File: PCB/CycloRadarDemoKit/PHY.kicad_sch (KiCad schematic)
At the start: 11 parts, among them U201 IP101GRI, Y201 Crystal_GND24

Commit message: PCB PHY WIP_1
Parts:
- added D201, D202: LED, symbol Device:LED
- added R206, R209: 5.1K(5%), symbol Device:R
- added R207, R208: R, symbol Device:R
- TP202: value TXER -> RXER
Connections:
- net +3V3: now also D201.2 (A), R206.2
- net GND: now also D202.1 (K), R209.2
- net at R203.2, U201.21 (RXER/INTR_32): now also TP202.1
- net LED0/PHY_AD0: now reaches U201.11 (LED0/PHY_AD0)
- net LED0/PHY_AD0: now also R206.1, R207.2
- net LED3/PHY_AD3: now reaches U201.12 (LED3/PHY_AD3)
- net LED3/PHY_AD3: now also R208.2, R209.1
- new net: D202.2 (A), R208.1
- new net: D201.1 (K), R207.1
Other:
- note added: "TODO: Choose LED on JLC - then decide on resistor"
- note added: "TODO: Choose RC components on JLC"
- note added: "pokračovať treba pinom 13, idem ACW"
- moved on the sheet: TP201, TP202

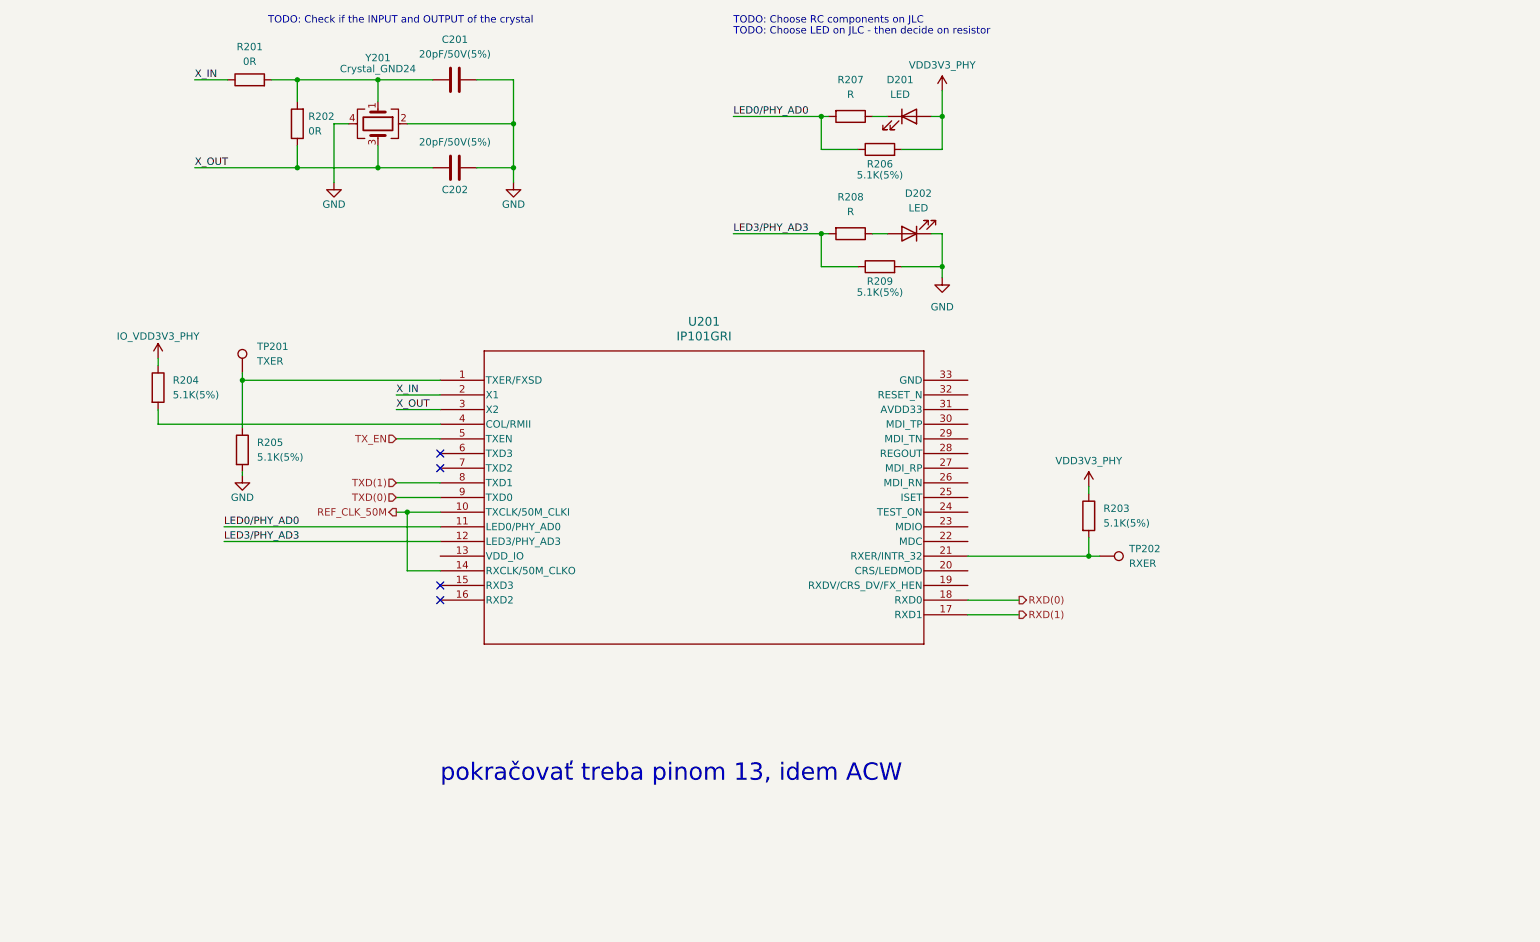
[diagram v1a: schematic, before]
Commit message: PCB WIP Started working on CP2102
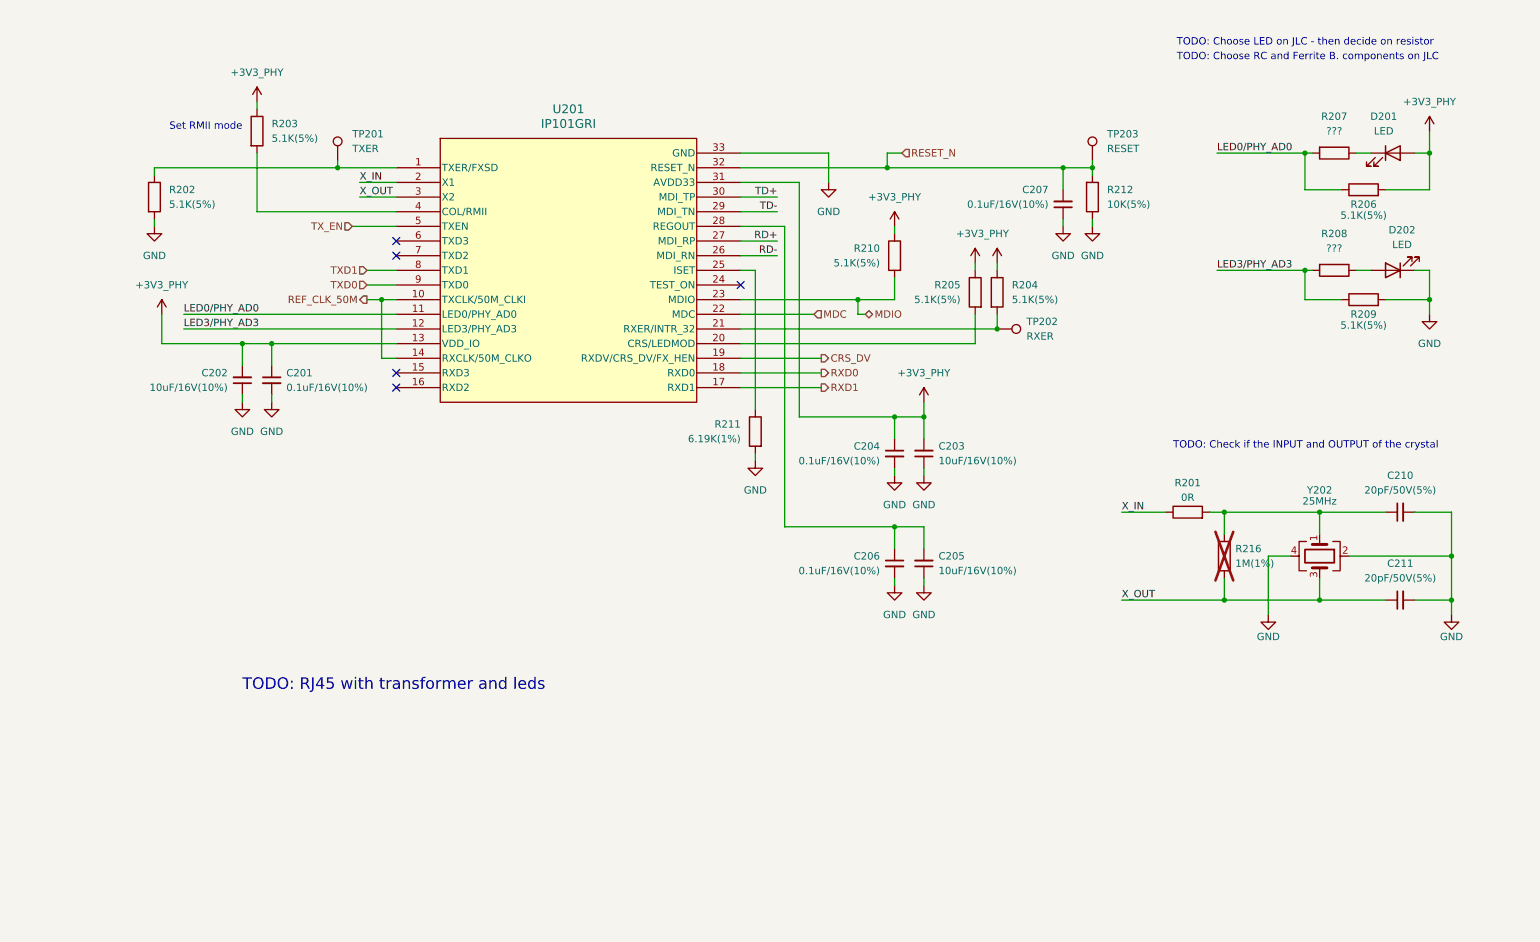
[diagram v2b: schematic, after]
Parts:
- removed C201, C202: 20pF/50V(5%), symbol Device:C
- removed Y201: Crystal_GND24, symbol Device:Crystal_GND24
- added C201, C204, C206, C207: 0.1uF/16V(10%), symbol Device:C_Small
- added C202, C203, C205: 10uF/16V(10%), symbol Device:C_Small
- added C210, C211: 20pF/50V(5%), symbol Device:C_Small
- added R210: 5.1K(5%), symbol Device:R
- added R211: 6.19K(1%), symbol Device:R
- added R212: 10K(5%), symbol Device:R
- added R216: 1M(1%), symbol Device:R
- added TP203: RESET, symbol Connector:TestPoint
- added Y202: 25MHz, symbol Device:Crystal_GND24
- R202: value 0R -> 5.1K(5%)
- R207, R208: value R -> ???
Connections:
- net +3V3 is gone; now on net +3V3_PHY: D201.2 (A), R203.1, R204.1, R206.2
- net GND: now also R202.2, U201.33 (GND), C201.2, C202.1, C203.1, C204.2, C205.1, C206.2, C207.1, C210.2, C211.2, R211.2, R212.1, Y202.2, Y202.4; no longer R205.2
- net X_OUT: now also C211.1, R216.1, Y202.3; no longer R202.1
- net at R201.2: now also C210.1, R216.2, Y202.1; no longer R202.2
- net at TP202.1, U201.21 (RXER/INTR_32): now also R204.2; no longer R203.2
- net at U201.4 (COL/RMII): now also R203.2; no longer R204.2
- net at TP201.1, U201.1 (TXER/FXSD): now also R202.1; no longer R205.1
- net +3V3_PHY: now reaches U201.13 (VDD_IO)
- net +3V3_PHY: now also R205.1, U201.31 (AVDD33), C201.1, C202.2, C203.2, C204.1, R210.1
- net CRS_DV: now reaches U201.19 (RXDV/CRS_DV/FX_HEN)
- net at U201.20 (CRS/LEDMOD): now also R205.2
- net MDC: now reaches U201.22 (MDC)
- net MDIO: now reaches U201.23 (MDIO)
- net MDIO: now also R210.2
- net at U201.25 (ISET): now also R211.1
- net RD-: now reaches U201.26 (MDI_RN)
- net RD+: now reaches U201.27 (MDI_RP)
- net at U201.28 (REGOUT): now also C205.2, C206.1
- net TD-: now reaches U201.29 (MDI_TN)
- net TD+: now reaches U201.30 (MDI_TP)
- net RESET_N: now reaches U201.32 (RESET_N)
- net RESET_N: now also C207.2, R212.2, TP203.1
- net RXD(0) renamed RXD0
- net RXD(1) renamed RXD1
- net TXD(0) renamed TXD0
- net TXD(1) renamed TXD1
- no-connect marks 4 -> 5
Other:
- note added: "Set RMII mode"
- note added: "TODO: Choose RC and Ferrite B. components on JLC"
- note added: "TODO: RJ45 with transformer and leds"
- note removed: "TODO: Choose RC components on JLC"
- note removed: "pokračovať treba pinom 13, idem ACW"
- company: (none) -> Alps Electric Czech, s.r.o.
- title: (none) -> Development module for Radar Safety Sensor
- moved on the sheet: D201, D202, R206, R207, R208, R209

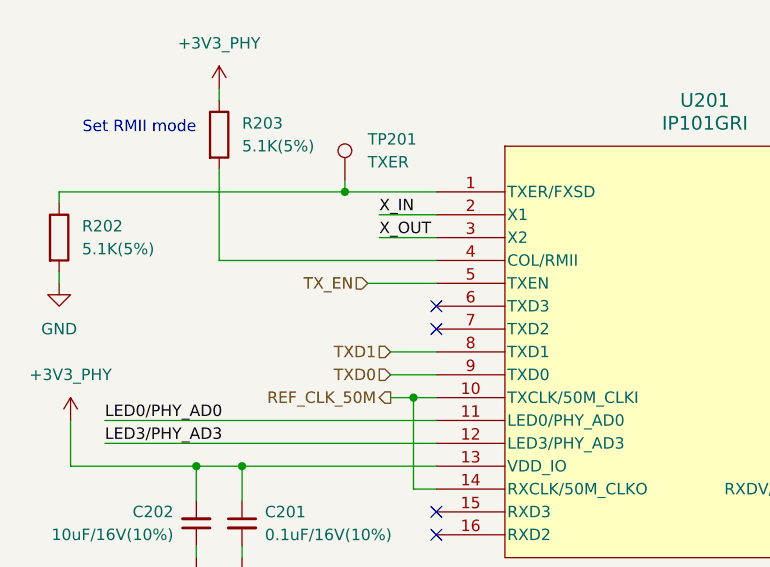
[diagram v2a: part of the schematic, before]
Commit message: Readme, PCB new symbol routed
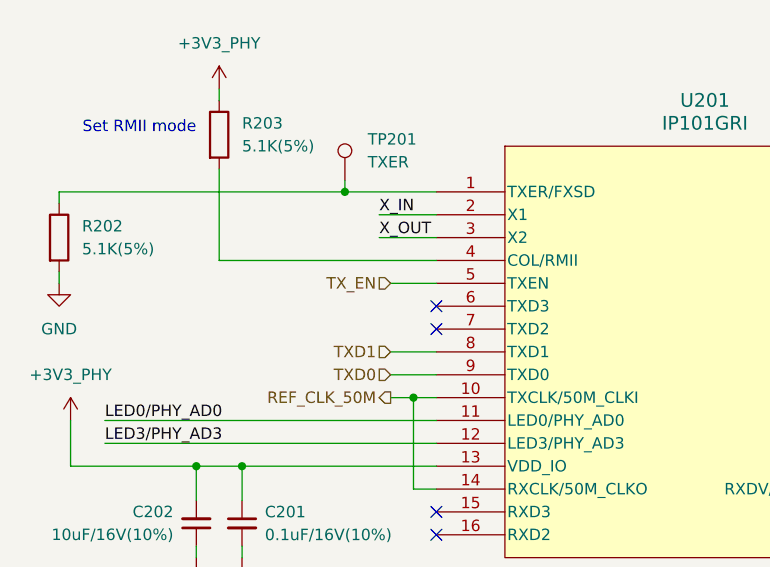
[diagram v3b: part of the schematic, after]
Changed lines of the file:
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@@
     (stroke (width 0) (type default))
   )
-  (wire (pts (xy 83.82 54.61) (xy 91.44 54.61))
+  (wire (pts (xy 86.36 54.61) (xy 91.44 54.61))
     (stroke (width 0) (type default))
   )
@@
     (effects (font (size 1.27 1.27)) (justify left bottom))
   )
-  (hierarchical_label "TX_EN" (shape input) (at 83.82 54.61 180) (fields_autoplaced)
+  (hierarchical_label "TX_EN" (shape input) (at 86.36 54.61 180) (fields_autoplaced)
     (effects (font (size 1.27 1.27)) (justify right))
   )

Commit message: PCB power manag. WIP
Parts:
- added R213: 0R, symbol Device:R
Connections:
- net X_OUT: now also R213.1; no longer C211.1, R216.1, Y202.3
- new net: C211.1, R213.2, R216.1, Y202.3
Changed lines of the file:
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@@
     (stroke (width 0) (type default))
   )
-  (wire (pts (xy 217.17 119.38) (xy 234.95 119.38))
+  (wire (pts (xy 232.41 119.38) (xy 234.95 119.38))
+    (stroke (width 0) (type default))
+  )
+  (wire (pts (xy 217.17 119.38) (xy 224.79 119.38))
     (stroke (width 0) (type default))
   )
@@
         )
       )
+    )
+  )
+  (symbol (lib_id "Device:R") (at 228.6 119.38 90) (unit 1)
+    (in_bom yes) (on_board yes) (dnp no)
+    (property "Reference" "R213" (at 228.6 114.3 90)
+      (effects (font (size 1.27 1.27)))
+    )
+    (property "Value" "0R" (at 228.6 116.84 90)
+      (effects (font (size 1.27 1.27)))
+    )
+    (property "Footprint" "" (at 228.6 121.158 90)
+      (effects (font (size 1.27 1.27)) hide)
+    )
+    (property "Datasheet" "~" (at 228.6 119.38 0)
+      (effects (font (size 1.27 1.27)) hide)
+    )
+    (pin "1")
+    (pin "2")
+    (instances
+      (project "CycloRadarDemoKit"
+        (path "/c2cd7ca4-4652-4b3d-a3a8-1cfa66cb11e9/8ae18a6c-482d-4e1c-94d1-12de0ef4fa68"
+          (reference "R213") (unit 1)
+        )
+      )

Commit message: Power management almost done
5V/3.3V changed to AP63203
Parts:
- renumbered C207 to C201, C201 to C203, C203 to C205, C210 to C206, C206 to C207, C205 to C208, C211 to C209, R203 to R201, R207 to R202, R206 to R203, R202 to R204, R212 to R205, R210 to R206, R208 to R207, R205 to R208, R204 to R209, R209 to R210, R201 to R212, R216 to R213, R213 to R214, TP203 to TP202, TP202 to TP203, Y202 to Y201

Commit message: RJ45 chose, leds connected
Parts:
- removed D201, D202: LED, symbol Device:LED
- removed R202, R207: ???, symbol Device:R
- removed R203: 5.1K(5%), symbol Device:R
- added C210, C211: 0.1uF/16V(10%), symbol Device:C_Small
- added C212, C213: 4.7nF/2kV(10%), symbol Device:C_Small
- added J201: ARJM11B1-009-AB-EW2, symbol Connector:RJ45_100Base-T
- added R208, R214: 5.1K(5%), symbol Device:R
- added R212: ???, symbol Device:R
- C201, C203, C204: value 0.1uF/16V(10%) -> 0.1uF/50V(10%); footprint (none) -> Capacitor_SMD:C_0603_1608Metric; LCSC (none) -> C14663
- C206: renamed from C207; value 0.1uF/16V(10%) -> 0.1uF/50V(10%); footprint (none) -> Capacitor_SMD:C_0603_1608Metric; LCSC (none) -> C14663
- R209: renamed from R212; footprint (none) -> Resistor_SMD:R_0805_2012Metric; LCSC (none) -> C17477
- R210: value 5.1K(5%) -> ???
- R213: renamed from R214; footprint (none) -> Resistor_SMD:R_0805_2012Metric; LCSC (none) -> C17477
- U201: LCSC (none) -> C703537
- Y201: footprint (none) -> Crystal:Crystal_SMD_3225-4Pin_3.2x2.5mm; LCSC (none) -> C124313
- renumbered C208 to C207, C206 to C208, R204 to R202, R205 to R203, R206 to R204, R208 to R205, R209 to R206, R211 to R207, R213 to R211
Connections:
- net +3V3_PHY: now also J201.P9, R208.2
- net GND: now also R210.1, C210.2, C211.2, C212.2, C213.2, R214.1; no longer R210.2
- net LED0/PHY_AD0: now also R208.1, R212.1
- net LED3/PHY_AD3: now also J201.P11, R214.2; no longer R210.1
- net RD+: now also J201.P3 (RD+)
- net RD-: now also J201.P6 (RD-)
- net TD+: now also J201.P1 (TD+)
- net TD-: now also J201.P2 (TD-)
- new net: C210.1, C211.1, J201.P4 (TCT), J201.P5 (RCT)
- new net: C212.1, C213.1, J201.P8
- new net: J201.P12, R210.2
- new net: J201.P10, R212.2
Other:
- note added: "Green"
- note added: "TODO: LED decide on resistor TODO: Select RJ45 footprint"
- note removed: "TODO: Choose LED on JLC - then decide on resistor"
- note removed: "TODO: Choose RC and Ferrite B. components on JLC"
- note removed: "TODO: RJ45 with transformer and leds"
- moved on the sheet: C208, C209, R209, R211, R213, Y201

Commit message: RJ45 footprint added
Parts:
- J201: footprint (none) -> Connector_RJ:RJ45_Abracon_ARJM11B1-009-AB-EW2_ABR
- R210: value ??? -> 120; footprint (none) -> Resistor_SMD:R_0603_1608Metric; LCSC (none) -> C22787
- R212: value ??? -> 100; footprint (none) -> Resistor_SMD:R_0603_1608Metric; LCSC (none) -> C22775
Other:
- note added: "Yellow"
- note removed: "TODO: LED decide on resistor TODO: Select RJ45 footprint"
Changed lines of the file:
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@@
     (effects (font (size 1.27 1.27)) (justify right bottom))
   )
-  (text "TODO:  LED decide on resistor\nTODO: Select RJ45 footprint"
-    (at 74.93 111.76 0)
-    (effects (font (size 1.27 1.27)) (justify left bottom))
+  (text "Yellow" (at 97.79 128.27 0)
+    (effects (font (size 1.27 1.27)) (justify right bottom))
   )
   (text "TODO: Check if the INPUT and OUTPUT of the crystal"
@@
       (effects (font (size 1.27 1.27)))
     )
-    (property "Value" "???" (at 101.6 127 90)
-      (effects (font (size 1.27 1.27)))
-    )
-    (property "Footprint" "" (at 101.6 129.032 90)
+    (property "Value" "120" (at 101.6 127 90)
+      (effects (font (size 1.27 1.27)))
+    )
+    (property "Footprint" "Resistor_SMD:R_0603_1608Metric" (at 101.6 129.032 90)
       (effects (font (size 1.27 1.27)) hide)
     )
@@
       (effects (font (size 1.27 1.27)) hide)
     )
+    (property "LCSC" "C22787" (at 101.6 130.81 90)
+      (effects (font (size 1.27 1.27)) hide)
+    )
     (pin "1")
     (pin "2")
@@
       (effects (font (size 1.27 1.27)))
     )
-    (property "Value" "???" (at 101.6 138.43 90)
-      (effects (font (size 1.27 1.27)))
-    )
-    (property "Footprint" "" (at 101.6 139.192 90)
+    (property "Value" "100" (at 101.6 138.43 90)
+      (effects (font (size 1.27 1.27)))
+    )
+    (property "Footprint" "Resistor_SMD:R_0603_1608Metric" (at 101.6 139.192 90)
       (effects (font (size 1.27 1.27)) hide)
     )
     (property "Datasheet" "~" (at 101.6 140.97 0)
+      (effects (font (size 1.27 1.27)) hide)
+    )
+    (property "LCSC" "C22775" (at 101.6 140.97 90)
       (effects (font (size 1.27 1.27)) hide)
     )
@@
       (effects (font (size 1.27 1.27)))
     )
-    (property "Footprint" "" (at 71.12 125.73 0)
-      (effects (font (size 1.27 1.27)) hide)
-    )
+    (property "Footprint" "Connector_RJ:RJ45_Abracon_ARJM11B1-009-AB-EW2_ABR" (at 71.12 125.73 0)
+      (effects (font (size 1.27 1.27)) hide)
+    )

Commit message: MPU added, power managemennt updated
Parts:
- added R201: 0R, Resistor_SMD:R_0805_2012Metric, symbol Device:R
- R211: renamed from R210; value 120 -> 270; LCSC C22787 -> C22966
- R213: renamed from R212; value 100 -> 220; LCSC C22775 -> C22962
- renumbered R201 to R202, R202 to R203, R203 to R204, R204 to R205, R205 to R206, R206 to R207, R207 to R208, R208 to R209, R209 to R210, R211 to R212, R213 to R214, R214 to R215
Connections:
- net +3V3_PHY: now also R201.1
- new net +3V3: R201.2
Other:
- moved on the sheet: C201, C202, C203, C204, C205, C206, C207, C208, C209, C210, C211, C212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
